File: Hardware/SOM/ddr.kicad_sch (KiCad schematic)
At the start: 15 parts, among them U2 AS4C256M16D3

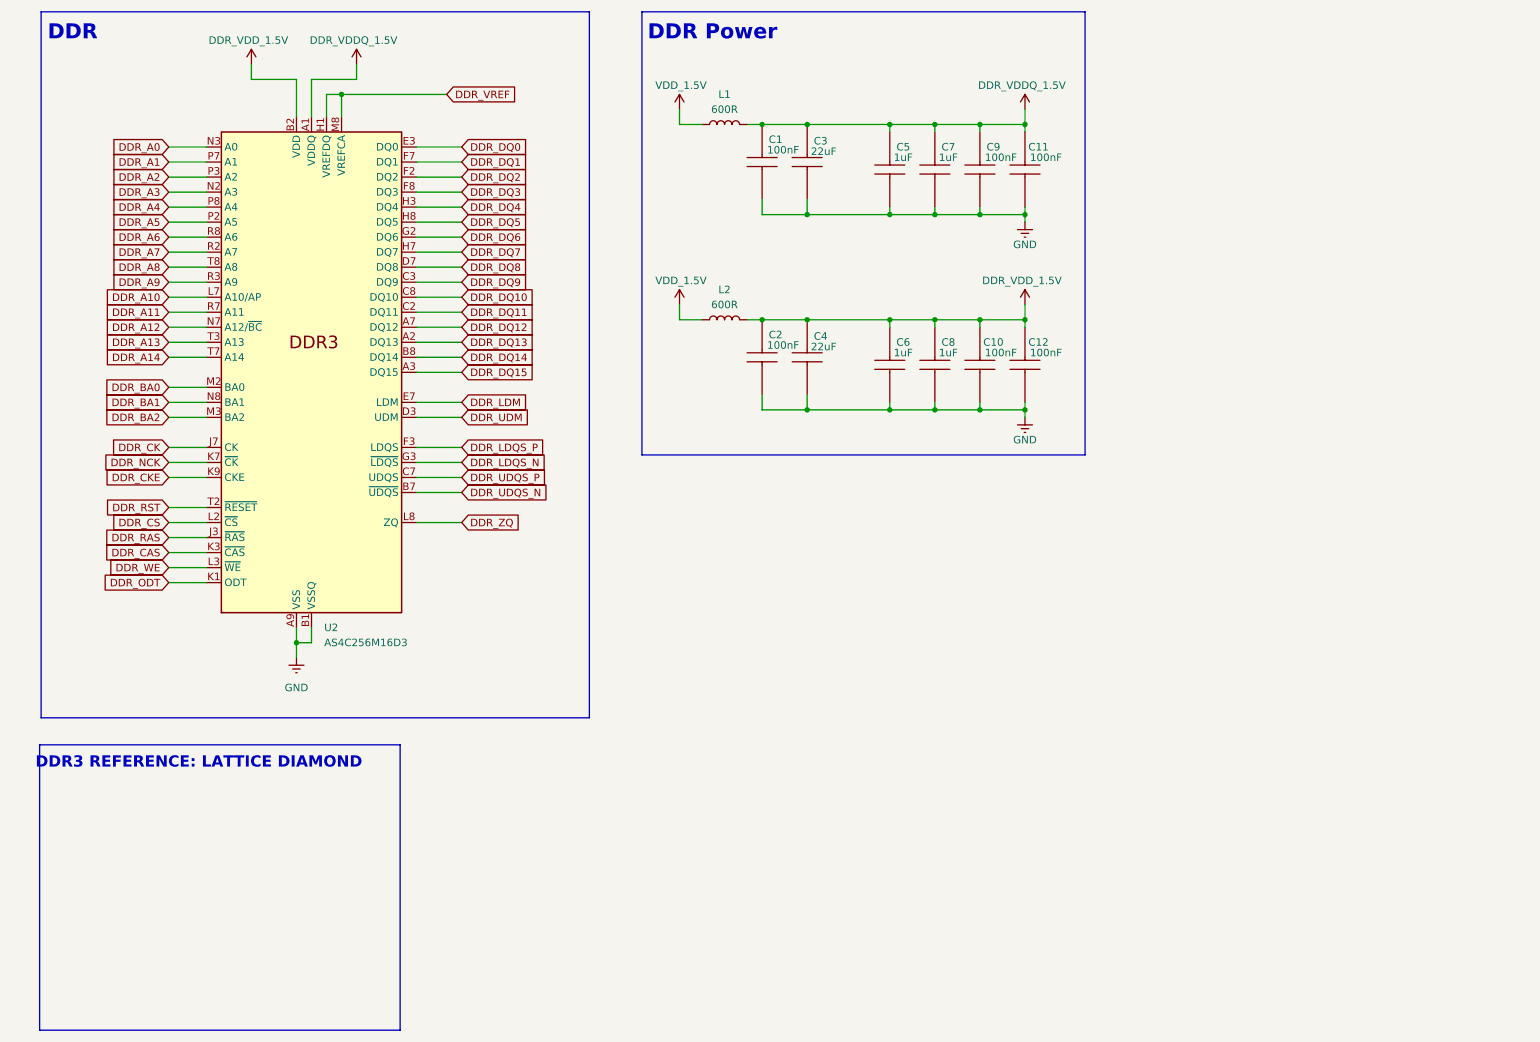
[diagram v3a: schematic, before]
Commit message: QSPI, banks IO decoupling
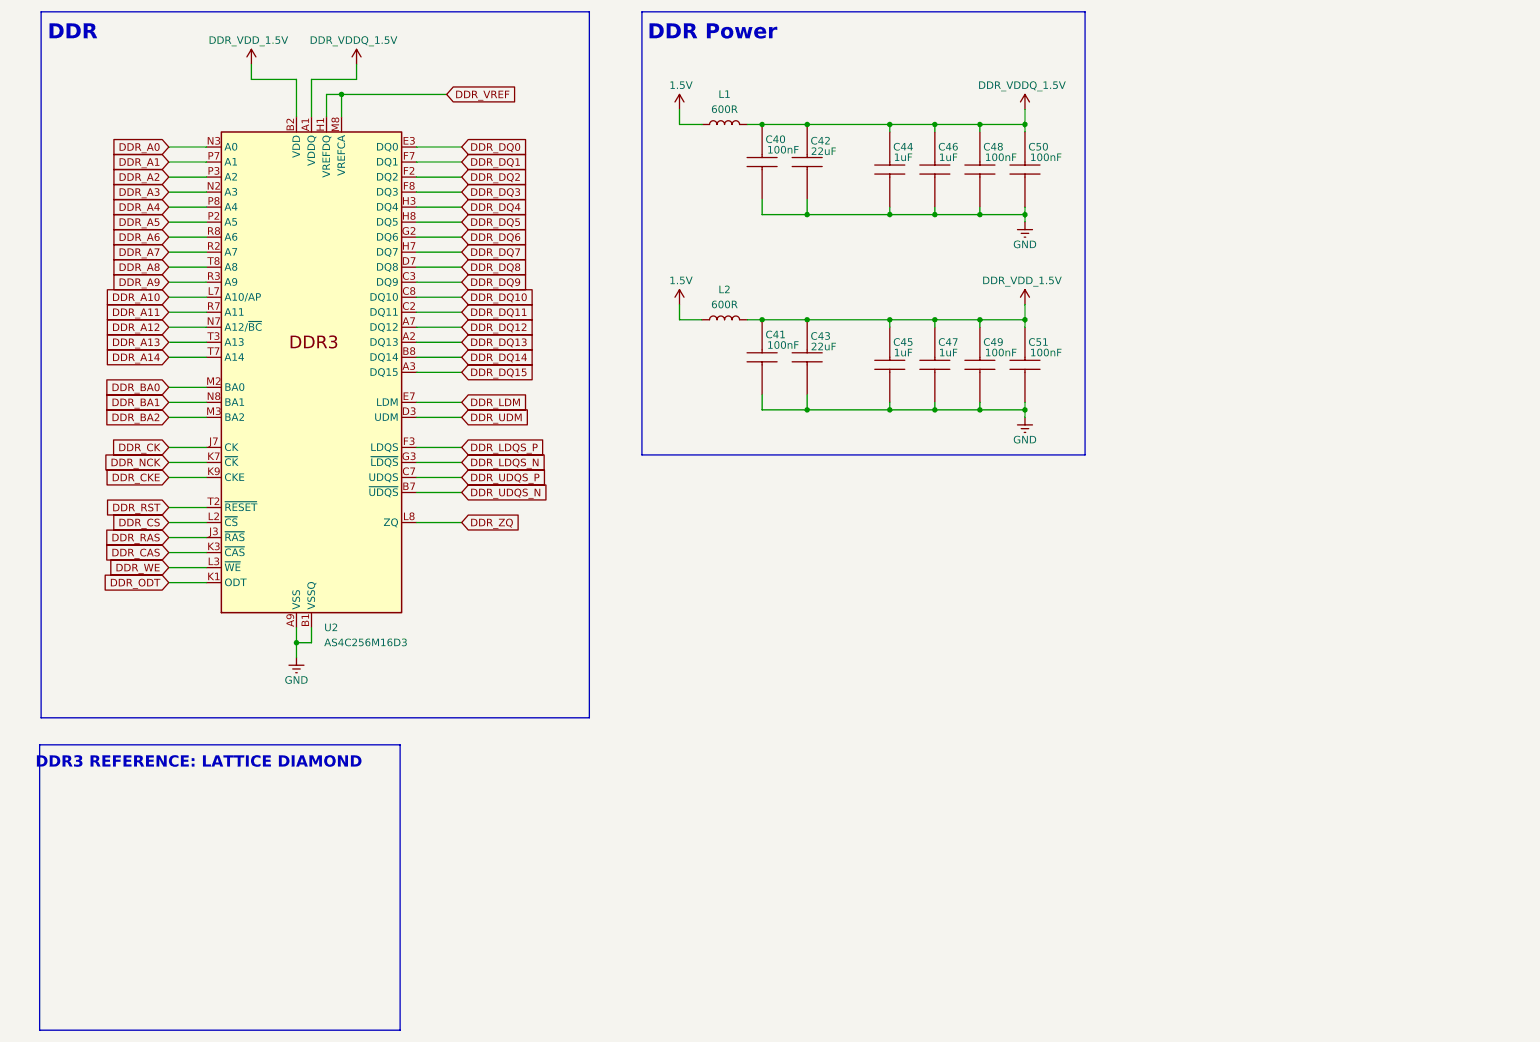
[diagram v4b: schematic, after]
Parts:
- renumbered C1 to C40, C2 to C41, C3 to C42, C4 to C43, C5 to C44, C6 to C45, C7 to C46, C8 to C47, C9 to C48, C10 to C49, C11 to C50, C12 to C51
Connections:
- net VDD_1.5V renamed 1.5V
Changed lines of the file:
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@@
 		(on_board yes)
 		(dnp no)
-		(property "Reference" "C1"
+		(property "Reference" "C40"
 			(at 148.336 43.18 90)
 			(effects
@@
 			(project "LFE5UM5G-85F_SOM"
 				(path "/de32abb0-ff3b-4c67-a91a-eed08140b1b2/70285655-daa5-4a1b-b29b-80c93a345d65"
-					(reference "C1")
+					(reference "C40")
 					(unit 1)
 				)
@@
 		(on_board yes)
 		(dnp no)
-		(property "Reference" "C9"
+		(property "Reference" "C48"
 			(at 185.166 44.45 90)
 			(effects
@@
 			(project "LFE5UM5G-85F_SOM"
 				(path "/de32abb0-ff3b-4c67-a91a-eed08140b1b2/70285655-daa5-4a1b-b29b-80c93a345d65"
-					(reference "C9")
+					(reference "C48")
 					(unit 1)
 				)
@@
 		(on_board yes)
 		(dnp no)
-		(property "Reference" "C6"
+		(property "Reference" "C45"
 			(at 169.926 77.47 90)
 			(effects
@@
 			(project "LFE5UM5G-85F_SOM"
 				(path "/de32abb0-ff3b-4c67-a91a-eed08140b1b2/70285655-daa5-4a1b-b29b-80c93a345d65"
-					(reference "C6")
+					(reference "C45")
 					(unit 1)
 				)
@@
 		(on_board yes)
 		(dnp no)
-		(property "Reference" "C10"
+		(property "Reference" "C49"
 			(at 185.166 77.47 90)
 			(effects
@@
 			(project "LFE5UM5G-85F_SOM"
 				(path "/de32abb0-ff3b-4c67-a91a-eed08140b1b2/70285655-daa5-4a1b-b29b-80c93a345d65"
-					(reference "C10")
+					(reference "C49")
 					(unit 1)
 				)
@@
 		(on_board yes)
 		(dnp no)
-		(fields_autoplaced yes)
-		(property "Reference" "#PWR02"
+		(property "Reference" "#PWR022"
 			(at 67.31 137.16 0)
 			(effects
@@
 		)
 		(property "Value" "GND"
-			(at 67.31 135.89 0)
+			(at 67.31 134.62 0)
 			(effects
 				(font
@@
 			(project "LFE5UM5G-85F_SOM"
 				(path "/de32abb0-ff3b-4c67-a91a-eed08140b1b2/70285655-daa5-4a1b-b29b-80c93a345d65"
-					(reference "#PWR02")
+					(reference "#PWR022")
 					(unit 1)
 				)
@@
 		(on_board yes)
 		(dnp no)
-		(property "Reference" "C11"
+		(property "Reference" "C50"
 			(at 192.786 44.45 90)
 			(effects
@@
 			(project "LFE5UM5G-85F_SOM"
 				(path "/de32abb0-ff3b-4c67-a91a-eed08140b1b2/70285655-daa5-4a1b-b29b-80c93a345d65"
-					(reference "C11")
+					(reference "C50")
 					(unit 1)
 				)
@@
 		(on_board yes)
 		(dnp no)
-		(property "Reference" "C3"
+		(property "Reference" "C42"
 			(at 155.956 43.434 90)
 			(effects
@@
 			(project "LFE5UM5G-85F_SOM"
 				(path "/de32abb0-ff3b-4c67-a91a-eed08140b1b2/70285655-daa5-4a1b-b29b-80c93a345d65"
-					(reference "C3")
+					(reference "C42")
 					(unit 1)
 				)
@@
 		(on_board yes)
 		(dnp no)
-		(property "Reference" "C2"
+		(property "Reference" "C41"
 			(at 148.336 76.2 90)
 			(effects
@@
 			(project "LFE5UM5G-85F_SOM"
 				(path "/de32abb0-ff3b-4c67-a91a-eed08140b1b2/70285655-daa5-4a1b-b29b-80c93a345d65"
-					(reference "C2")
+					(reference "C41")
 					(unit 1)
 				)
@@
 		(on_board yes)
 		(dnp no)
-		(property "Reference" "#PWR08"
+		(property "Reference" "#PWR028"
 			(at 190.5 74.93 0)
 			(effects
@@
 			(project "LFE5UM5G-85F_SOM"
 				(path "/de32abb0-ff3b-4c67-a91a-eed08140b1b2/70285655-daa5-4a1b-b29b-80c93a345d65"
-					(reference "#PWR08")
+					(reference "#PWR028")
 					(unit 1)
 				)
@@
 		(on_board yes)
 		(dnp no)
-		(property "Reference" "#PWR07"
+		(property "Reference" "#PWR027"
 			(at 190.5 63.5 0)
 			(effects
@@
 			(project "LFE5UM5G-85F_SOM"
 				(path "/de32abb0-ff3b-4c67-a91a-eed08140b1b2/70285655-daa5-4a1b-b29b-80c93a345d65"
-					(reference "#PWR07")
+					(reference "#PWR027")
 					(unit 1)
 				)
@@
 		(on_board yes)
 		(dnp no)
-		(property "Reference" "#PWR01"
+		(property "Reference" "#PWR021"
 			(at 59.69 34.29 0)
 			(effects
@@
 			(project "LFE5UM5G-85F_SOM"
 				(path "/de32abb0-ff3b-4c67-a91a-eed08140b1b2/70285655-daa5-4a1b-b29b-80c93a345d65"
-					(reference "#PWR01")
+					(reference "#PWR021")
 					(unit 1)
 				)
@@
 		(on_board yes)
 		(dnp no)
-		(property "Reference" "#PWR04"
+		(property "Reference" "#PWR024"
 			(at 132.08 41.91 0)
 			(effects
@@
 			)
 		)
-		(property "Value" "VDD_1.5V"
+		(property "Value" "1.5V"
 			(at 132.334 34.036 0)
 			(effects
@@
 			(project "LFE5UM5G-85F_SOM"
 				(path "/de32abb0-ff3b-4c67-a91a-eed08140b1b2/70285655-daa5-4a1b-b29b-80c93a345d65"
-					(reference "#PWR04")
+					(reference "#PWR024")
 					(unit 1)
 				)
@@
 		(on_board yes)
 		(dnp no)
-		(property "Reference" "C12"
+		(property "Reference" "C51"
 			(at 192.786 77.47 90)
 			(effects
@@
 			(project "LFE5UM5G-85F_SOM"
 				(path "/de32abb0-ff3b-4c67-a91a-eed08140b1b2/70285655-daa5-4a1b-b29b-80c93a345d65"
-					(reference "C12")
+					(reference "C51")
 					(unit 1)
 				)
@@
 		(on_board yes)
 		(dnp no)
-		(property "Reference" "#PWR06"
+		(property "Reference" "#PWR026"
 			(at 190.5 41.91 0)
 			(effects
@@
 			(project "LFE5UM5G-85F_SOM"
 				(path "/de32abb0-ff3b-4c67-a91a-eed08140b1b2/70285655-daa5-4a1b-b29b-80c93a345d65"
-					(reference "#PWR06")
+					(reference "#PWR026")
 					(unit 1)
 				)
@@
 		(on_board yes)
 		(dnp no)
-		(property "Reference" "C4"
+		(property "Reference" "C43"
 			(at 155.956 76.454 90)
 			(effects
@@
 			(project "LFE5UM5G-85F_SOM"
 				(path "/de32abb0-ff3b-4c67-a91a-eed08140b1b2/70285655-daa5-4a1b-b29b-80c93a345d65"
-					(reference "C4")
+					(reference "C43")
 					(unit 1)
 				)
@@
 		(on_board yes)
 		(dnp no)
-		(property "Reference" "#PWR09"
+		(property "Reference" "#PWR029"
 			(at 190.5 96.52 0)
 			(effects
@@
 			(project "LFE5UM5G-85F_SOM"
 				(path "/de32abb0-ff3b-4c67-a91a-eed08140b1b2/70285655-daa5-4a1b-b29b-80c93a345d65"
-					(reference "#PWR09")
+					(reference "#PWR029")
 					(unit 1)
 				)
@@
 		(on_board yes)
 		(dnp no)
-		(property "Reference" "C5"
+		(property "Reference" "C44"
 			(at 169.926 44.45 90)
 			(effects
@@
 			(project "LFE5UM5G-85F_SOM"
 				(path "/de32abb0-ff3b-4c67-a91a-eed08140b1b2/70285655-daa5-4a1b-b29b-80c93a345d65"
-					(reference "C5")
+					(reference "C44")
 					(unit 1)
 				)
@@
 		(on_board yes)
 		(dnp no)
-		(property "Reference" "#PWR03"
+		(property "Reference" "#PWR023"
 			(at 77.47 34.29 0)
 			(effects
@@
 			(project "LFE5UM5G-85F_SOM"
 				(path "/de32abb0-ff3b-4c67-a91a-eed08140b1b2/70285655-daa5-4a1b-b29b-80c93a345d65"
-					(reference "#PWR03")
+					(reference "#PWR023")
 					(unit 1)
 				)
@@
 		(on_board yes)
 		(dnp no)
-		(property "Reference" "C8"
+		(property "Reference" "C47"
 			(at 177.546 77.47 90)
 			(effects
@@
 			(project "LFE5UM5G-85F_SOM"
 				(path "/de32abb0-ff3b-4c67-a91a-eed08140b1b2/70285655-daa5-4a1b-b29b-80c93a345d65"
-					(reference "C8")
+					(reference "C47")
 					(unit 1)
 				)
@@
 		(on_board yes)
 		(dnp no)
-		(property "Reference" "C7"
+		(property "Reference" "C46"
 			(at 177.546 44.45 90)
 			(effects
@@
 			(project "LFE5UM5G-85F_SOM"
 				(path "/de32abb0-ff3b-4c67-a91a-eed08140b1b2/70285655-daa5-4a1b-b29b-80c93a345d65"
-					(reference "C7")
+					(reference "C46")
 					(unit 1)
 				)
@@
 		(on_board yes)
 		(dnp no)
-		(property "Reference" "#PWR05"
+		(property "Reference" "#PWR025"
 			(at 132.08 74.93 0)
 			(effects
@@
 			)
 		)
-		(property "Value" "VDD_1.5V"
+		(property "Value" "1.5V"
 			(at 132.334 67.056 0)
 			(effects
@@
 			(project "LFE5UM5G-85F_SOM"
 				(path "/de32abb0-ff3b-4c67-a91a-eed08140b1b2/70285655-daa5-4a1b-b29b-80c93a345d65"
-					(reference "#PWR05")
-					(unit 1)
-				)
+					(reference "#PWR025")
+					(unit 1)
+				)

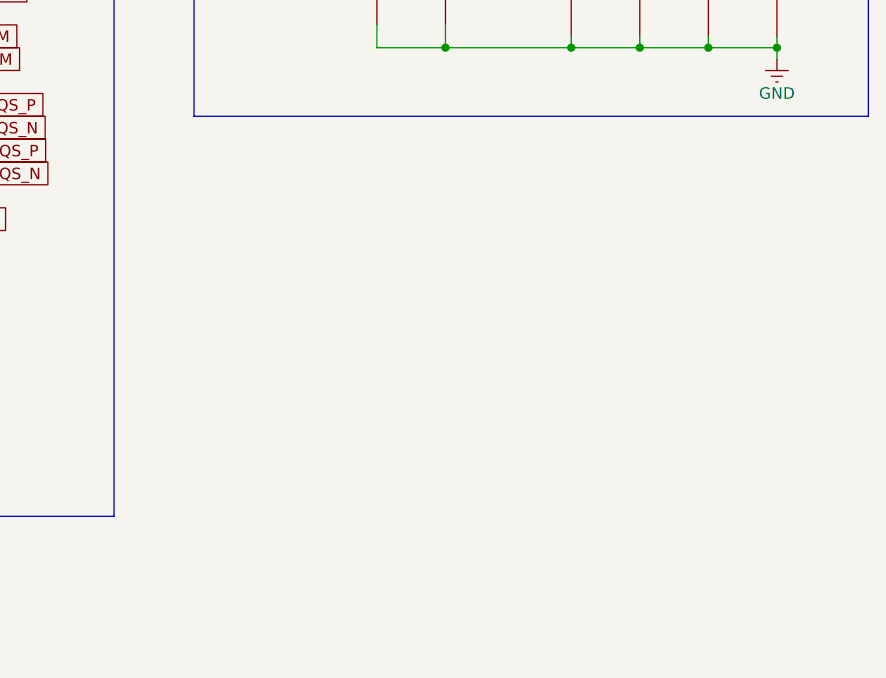
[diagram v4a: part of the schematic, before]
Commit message: DDR clock termination
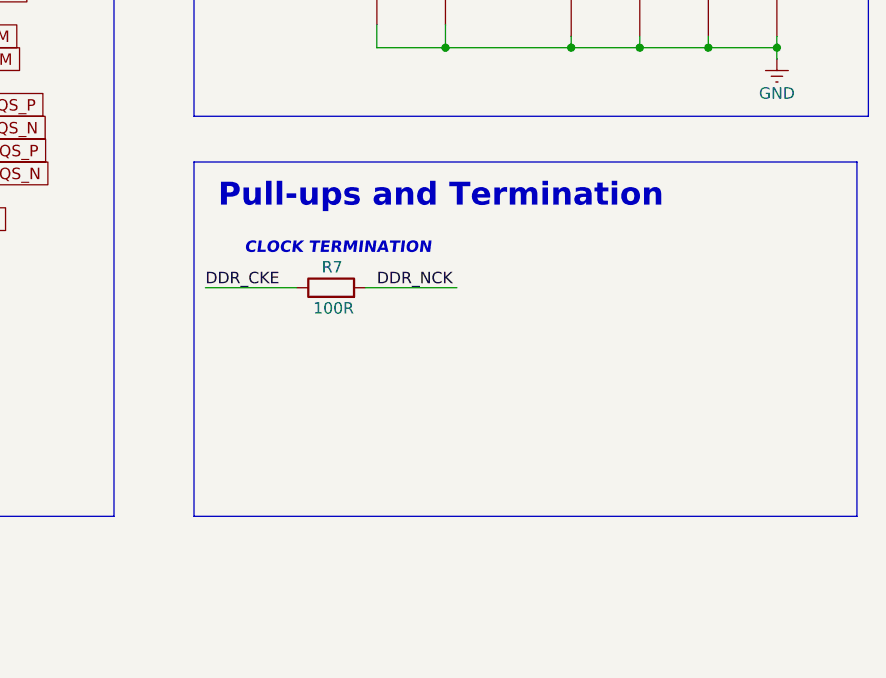
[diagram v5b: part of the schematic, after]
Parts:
- added R7: 100R, Resistor_SMD:R_0402_1005Metric, symbol Device:R
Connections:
- net DDR_CKE: now also R7.1
- net DDR_NCK: now also R7.2
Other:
- note added: "CLOCK TERMINATION"
- note added: "Pull-ups and Termination"
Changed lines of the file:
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@@
 	)
 	(rectangle
+		(start 125.73 101.6)
+		(end 199.39 140.97)
+		(stroke
+			(width 0)
+			(type default)
+		)
+		(fill
+			(type none)
+		)
+	)
+	(rectangle
 		(start 24.13 21.59)
 		(end 116.84 140.97)
@@
 		)
 	)
+	(text "CLOCK TERMINATION"
+		(exclude_from_sim no)
+		(at 141.732 111.252 0)
+		(effects
+			(font
+				(size 1.27 1.27)
+				(thickness 0.254)
+				(bold yes)
+				(italic yes)
+				(color 0 132 0 1)
+			)
+		)
+	)
 	(text "DDR"
 		(exclude_from_sim no)
@@
 		)
 	)
+	(text "Pull-ups and Termination"
+		(exclude_from_sim no)
+		(at 153.162 105.41 0)
+		(effects
+			(font
+				(size 2.54 2.54)
+				(thickness 0.254)
+				(bold yes)
+			)
+		)
+	)
 	(text "DDR Power"
 		(exclude_from_sim no)
@@
 	(wire
 		(pts
+			(xy 127 115.57) (xy 137.16 115.57)
+		)
+		(stroke
+			(width 0)
+			(type default)
+		)
+	)
+	(wire
+		(pts
 			(xy 190.5 88.9) (xy 182.88 88.9)
 		)
@@
 	(wire
 		(pts
+			(xy 144.78 115.57) (xy 154.94 115.57)
+		)
+		(stroke
+			(width 0)
+			(type default)
+		)
+	)
+	(wire
+		(pts
 			(xy 182.88 40.64) (xy 182.88 41.91)
 		)
@@
 		)
 	)
+	(label "DDR_NCK"
+		(at 146.05 115.57 0)
+		(effects
+			(font
+				(size 1.27 1.27)
+			)
+			(justify left bottom)
+		)
+	)
+	(label "DDR_CKE"
+		(at 127 115.57 0)
+		(effects
+			(font
+				(size 1.27 1.27)
+			)
+			(justify left bottom)
+		)
+	)
 	(global_label "DDR_DQ15"
 		(shape input)
@@
 					(unit 1)
 				)
+			)
+		)
+	)
+	(symbol
+		(lib_id "Device:R")
+		(at 140.97 115.57 90)
+		(unit 1)
+		(exclude_from_sim no)
+		(in_bom yes)
+		(on_board yes)
+		(dnp no)
+		(property "Reference" "R7"
+			(at 142.24 113.284 90)
+			(effects
+				(font
+					(size 1.27 1.27)
+				)
+				(justify left)
+			)
+		)
+		(property "Value" "100R"
+			(at 143.51 117.856 90)
+			(effects
+				(font
+					(size 1.27 1.27)
+				)
+				(justify left)
+			)
+		)
+		(property "Footprint" "Resistor_SMD:R_0402_1005Metric"
+			(at 140.97 117.348 90)
+			(effects
+				(font
+					(size 1.27 1.27)
+				)
+				(hide yes)
+			)
+		)
+		(property "Datasheet" "~"
+			(at 140.97 115.57 0)
+			(effects
+				(font
+					(size 1.27 1.27)
+				)
+				(hide yes)
+			)
+		)
+		(property "Description" "Resistor"
+			(at 140.97 115.57 0)
+			(effects
+				(font
+					(size 1.27 1.27)
+				)
+				(hide yes)
+			)
+		)
+		(property "Manufacturer" "Würth Elektronik"
+			(at 140.97 115.57 0)
+			(effects
+				(font
+					(size 1.27 1.27)
+				)
+				(hide yes)
+			)
+		)
+		(property "MPN" "560112110022"
+			(at 140.97 115.57 0)
+			(effects
+				(font
+					(size 1.27 1.27)
+				)
+				(hide yes)
+			)
+		)
+		(pin "1"
+		)
+		(pin "2"
+		)
+		(instances
+			(project "LFE5UM5G-85F_SOM"
+				(path "/de32abb0-ff3b-4c67-a91a-eed08140b1b2/70285655-daa5-4a1b-b29b-80c93a345d65"
+					(reference "R7")
+					(unit 1)
+				)
